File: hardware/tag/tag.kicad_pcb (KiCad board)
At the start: 2 copper layers, 50 x 52 mm, 109 parts, among them J1 USB_C_Receptacle_USB2.0_16P, J2 BATTERY, J3 UART, J4 I2C, J5 STM SWD, J6 ADC, J7 BLE SWD, J8 SOURCE, SW1 RESET, SW2 BOOT, SW3 USER, U1 ICM-45686, U2 TPS63070RNMR, U3 BQ24075RGT, U4 USBLC6-2SC6, U5 FSC-BT630, U6 STM32F411CEUx, U7 DWM1000, Y1 NX3215SA-32.768kHz(DNP), Y2 NX3225SA-24MHz

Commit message: refactor(hw): iterate on tag rev 0.2 design
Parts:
- removed C14: 22u, Capacitor_SMD:C_0805_2012Metric_Pad1.18x1.45mm_HandSolder
- removed C5: 1u, Capacitor_SMD:C_0805_2012Metric_Pad1.18x1.45mm_HandSolder
- removed C6, C7: 4.7u, Capacitor_SMD:C_0805_2012Metric_Pad1.18x1.45mm_HandSolder
- removed D1: RED, LED_SMD:LED_0603_1608Metric_Pad1.05x0.95mm_HandSolder
- removed D2: YELLOW, LED_SMD:LED_0603_1608Metric_Pad1.05x0.95mm_HandSolder
- removed R18, R9: 6k, Resistor_SMD:R_0603_1608Metric_Pad0.98x0.95mm_HandSolder
- removed R2: 3.1k, Resistor_SMD:R_0603_1608Metric_Pad0.98x0.95mm_HandSolder
- removed R3: 3.56k, Resistor_SMD:R_0603_1608Metric_Pad0.98x0.95mm_HandSolder
- removed R8: 10k, Resistor_SMD:R_0603_1608Metric_Pad0.98x0.95mm_HandSolder
- removed U3: BQ24075RGT, Package_DFN_QFN:VQFN-16-1EP_3x3mm_P0.5mm_EP1.6x1.6mm
- added C10: 1u, Capacitor_SMD:C_0805_2012Metric_Pad1.18x1.45mm_HandSolder, F.Cu at (51.0, 91.2)
- added C12: DNP, Capacitor_SMD:C_01005_0402Metric, F.Cu at (79.7, 74.7)
- added C34: 47n, Capacitor_SMD:C_0603_1608Metric, F.Cu at (47.7, 94.0)
- added C35: 4.7u, Capacitor_SMD:C_0805_2012Metric, F.Cu at (45.0, 95.0)
- added C36: 20u, Capacitor_SMD:C_0805_2012Metric, F.Cu at (56.4, 96.2)
- added C37: 10u, Capacitor_SMD:C_0805_2012Metric, F.Cu at (45.0, 99.1)
- added C8: DNP, Capacitor_SMD:C_01005_0402Metric, F.Cu at (79.7, 77.2)
- added D9: YELLOW, LED_SMD:LED_0603_1608Metric_Pad1.05x0.95mm_HandSolder, F.Cu at (51.7, 87.0)
- added J6: BLE_Conn, Connector_Coaxial:U.FL_Hirose_U.FL-R-SMT-1_Vertical, F.Cu at (76.8, 78.0)
- added L2: DNP, Inductor_SMD:L_0402_1005Metric, F.Cu at (79.9, 76.0)
- added L3: 1u, Inductor_SMD:L_Sunlord_SWPA4020S, F.Cu at (60.0, 91.2)
- added R25: 2.2k, Resistor_SMD:R_0603_1608Metric_Pad0.98x0.95mm_HandSolder, F.Cu at (48.0, 87.0)
- added R26: 10K, Resistor_SMD:R_0603_1608Metric_Pad0.98x0.95mm_HandSolder, F.Cu at (52.2, 98.2)
- added R27: DNP, Resistor_SMD:R_0603_1608Metric_Pad0.98x0.95mm_HandSolder, F.Cu at (47.7, 96.0)
- added U8: BQ25628RYKR, Other_Footprint:IC_BQ25628RYKR, F.Cu at (51.6, 95.4)
- C15: value DNP -> 22u
- D3: value YELLOW -> GREEN
- D4: value GREEN -> RED
- SW2: value BOOT -> PWR; footprint Button_Switch_SMD:SW_SPDT_PCM12 -> Button_Switch_SMD:SW_Push_1P1T-MP_NO_Horizontal_Alps_SKRTLAE010
- U5: footprint Other_Footprint:FSC-BT630 -> other_footprint:FSC-BT630
- moved SW2 22.1 mm to (57.4, 100.5), turned to 0 degrees
- moved R14 18.2 mm to (56.0, 85.5)
- moved TP3 7.84 mm to (78.0, 90.0)
- moved TP6 6.78 mm to (63.6, 91.1)
- moved D8 5.38 mm to (72.2, 76.1), turned to 90 degrees
- moved C1 4.32 mm to (62.4, 96.0), turned to -90 degrees
- moved R5 4.04 mm to (64.6, 99.4)
- moved C26 3.95 mm to (71.9, 60.5), turned to 0 degrees
- moved C4 3.68 mm to (64.3, 94.2)
- moved C15 3.64 mm to (73.8, 90.2)
- moved C11 3.63 mm to (73.7, 95.1)
- moved C13 3.63 mm to (73.7, 92.7)
- moved R10 3.63 mm to (73.7, 97.4)
- moved R11 3.63 mm to (73.7, 99.8)
- moved C27 3.56 mm to (72.1, 58.7), turned to 0 degrees
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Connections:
- net /SYS renamed SYS
- R14 pad 1: Net-(SW2-B) -> GND
- R19 pad 2: Net-(U5-P0.02/AIN0) -> Net-(U5-P0.03)
- SW2 pad 2: Net-(SW2-B) -> Net-(R26-Pad1)
- U5 pad 1: +3.3V -> /BLE_RX
- U5 pad 10: GND -> /BLE_SWDIO
- U5 pad 11: Net-(U5-P0.02/AIN0) -> unconnected-(U5-P0.30-Pad11)
- U5 pad 15: unconnected-(U5-P0.06-Pad15) -> Net-(U5-P0.03)
- U5 pad 19: unconnected-(U5-P0.10/NFC2-Pad19) -> GND
- U5 pad 20: unconnected-(U5-P0.11-Pad20) -> Net-(U5-EXT_ANT)
- U5 pad 3: /BLE_RX -> unconnected-(U5-I2C_SDA-Pad3)
- U5 pad 7: /BLE_SWDCLK -> +3.3V
- U5 pad 8: /BLE_SWDIO -> GND
- U5 pad 9: GND -> /BLE_SWDCLK
- U6 pad 29: /PA8 / TIM1_CH1 -> /PM_SCL
- U6 pad 38: /PA15 / TIM2_CH1 -> /LED_PM
- U6 pad 40: /PB4/TIM3_CH1 -> /PM_SDA
- U6 pad 42: /PB6 / TIM4_CH1 -> unconnected-(U6-PB6-Pad42)
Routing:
- net /PM_SCL: track 0.00 -> 25.3 mm, vias 0 -> 2
- net SYS: track 30.8 -> 9.78 mm, vias 0 -> 6
- net Net-(U6-BOOT0): track 24.2 -> 3.25 mm, vias 2 -> 0
- net /PM_SDA: track 0.00 -> 15.2 mm, vias 0 -> 2
- net /PGOOD: track 14.8 -> 0.00 mm, vias 2 -> 0
- net /CHG: track 10.9 -> 0.00 mm, vias 2 -> 0
- net /LED_PM: track 0.00 -> 10.1 mm
- net GND: track 25.0 -> 16.1 mm, vias 321 -> 299
- net +3.3V: track 221.2 -> 214.4 mm
- net +BATT: track 9.33 -> 3.43 mm, vias 0 -> 12
- net Net-(U8-REGN): track 0.00 -> 5.55 mm
- net Net-(R26-Pad1): track 0.00 -> 5.43 mm
- net Net-(U5-P0.02/AIN0): track 4.68 -> 0.00 mm
- net Net-(U8-SW): track 0.00 -> 4.20 mm, vias 0 -> 2
- net Net-(U8-BTST): track 0.00 -> 3.59 mm
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- added copper zone on B.Cu, net +BATT
- added copper zone on F.Cu, net +BATT
- added copper zone on F.Cu, net Net-(U8-SW)
- added copper zone on B.Cu, net SYS
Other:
- board text added: "${REFERENCE}"
- board text added: "3V3 RX TX GND"
- board text added: "BOARD: TAG REV v1.1"
- board text removed: "BOARD: TAG REV v1.0"
- board text removed: "GND TX RX 3V3"

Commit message: update(hw): release tag revision 0.2
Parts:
- removed the C10 at (51.0, 91.2)
- removed the C15 at (73.8, 90.2)
- removed the C3 at (60.4, 96.0)
- removed C34: 47n, Capacitor_SMD:C_0603_1608Metric
- removed C35: 4.7u, Capacitor_SMD:C_0805_2012Metric
- removed C36: 20u, Capacitor_SMD:C_0805_2012Metric
- removed C37: 10u, Capacitor_SMD:C_0805_2012Metric
- removed L3: 1u, Inductor_SMD:L_Sunlord_SWPA4020S
- removed the R26 at (52.2, 98.2)
- removed R27: DNP, Resistor_SMD:R_0603_1608Metric_Pad0.98x0.95mm_HandSolder
- removed the SW2 at (57.4, 100.5)
- removed the TP6 at (63.6, 91.1)
- removed the U8 at (51.6, 95.4)
- added C14: 22u, Capacitor_SMD:C_0805_2012Metric_Pad1.18x1.45mm_HandSolder, F.Cu at (73.8, 90.2)
- added C4: 100n, Capacitor_SMD:C_0603_1608Metric_Pad1.08x0.95mm_HandSolder, F.Cu at (46.1, 96.2)
- added C6: 1u, Capacitor_SMD:C_0805_2012Metric_Pad1.18x1.45mm_HandSolder, F.Cu at (55.0, 90.6)
- added C7: 1u, Capacitor_SMD:C_0603_1608Metric_Pad1.08x0.95mm_HandSolder, F.Cu at (62.7, 94.0)
- added C8: 4.7u, Capacitor_SMD:C_0805_2012Metric_Pad1.18x1.45mm_HandSolder, F.Cu at (50.0, 98.6)
- added C9: 10u, Capacitor_SMD:C_0805_2012Metric_Pad1.18x1.45mm_HandSolder, F.Cu at (57.7, 92.6)
- added Q1: AO664, Package_SO:TSOP-6_1.65x3.05mm_P0.95mm, F.Cu at (57.7, 95.5)
- added R12: 100k, Resistor_SMD:R_0603_1608Metric_Pad0.98x0.95mm_HandSolder, F.Cu at (61.0, 94.0)
- added R13: 10k, Resistor_SMD:R_0603_1608Metric_Pad0.98x0.95mm_HandSolder, F.Cu at (62.0, 91.5)
- added R14: 10k, Resistor_SMD:R_0603_1608Metric_Pad0.98x0.95mm_HandSolder, F.Cu at (60.2, 97.8)
- added R5: 3.1k, Resistor_SMD:R_0603_1608Metric_Pad0.98x0.95mm_HandSolder, F.Cu at (62.0, 90.0)
- added R6: 3.56k, Resistor_SMD:R_0603_1608Metric_Pad0.98x0.95mm_HandSolder, F.Cu at (51.4, 92.4)
- added R8: 10k, Resistor_SMD:R_0603_1608Metric_Pad0.98x0.95mm_HandSolder, F.Cu at (49.0, 93.3)
- added SW1: PWR, Button_Switch_SMD:SW_Push_1P1T-MP_NO_Horizontal_Alps_SKRTLAE010, F.Cu at (56.0, 100.3)
- added TP3: VSYS, TestPoint:TestPoint_Pad_D1.5mm, F.Cu at (58.5, 89.8)
- added U1: MAX17048G_T10, Package_SON:SON-8-1EP_3x2mm_P0.5mm_EP1.4x1.6mm, F.Cu at (46.6, 93.5)
- added U5: BQ24075RGT, Package_DFN_QFN:VQFN-16-1EP_3x3mm_P0.5mm_EP1.6x1.6mm, F.Cu at (53.3, 95.5)
- D3: value GREEN -> YELLOW
- D4: renamed from D9; value YELLOW -> GREEN
- D5: renamed from D4; value RED -> GREEN
- J9: renamed from J6; value ADC -> I2C
- TP2: renamed from TP3; footprint TestPoint:TestPoint_Pad_D2.0mm -> TestPoint:TestPoint_Pad_1.5x1.5mm
- TP5: renamed from TP4; footprint TestPoint:TestPoint_Pad_D2.0mm -> TestPoint:TestPoint_Pad_1.5x1.5mm
- moved C2 5.82 mm to (63.9, 98.0)
- moved C15 3.04 mm to (43.0, 74.4), turned to 180 degrees
- moved TP16 2.19 mm to (39.5, 69.8)
- moved TP7 2.16 mm to (45.4, 98.3)
- moved J4 2.00 mm to (35.0, 92.5), turned to 90 degrees
- moved C1 2.00 mm to (62.0, 98.0)
- moved R1 1.58 mm to (67.7, 99.5)
- moved R11 1.53 mm to (69.3, 99.5)
- moved C10 1.51 mm to (45.6, 75.1), turned to -90 degrees
- moved C5 1.49 mm to (70.9, 99.5)
- moved R2 1.49 mm to (66.1, 99.5)
- moved J6 1.45 mm to (78.7, 84.8)
- moved J1 1.38 mm to (34.0, 79.5)
- moved R3 1.38 mm to (40.3, 84.5)
- moved R4 1.38 mm to (40.3, 75.1)
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- renumbered C31 to C10, C13 to C12, C32 to C13, C33 to C15, C27 to C16, C26 to C17, C16 to C18, C17 to C19, C18 to C20, C19 to C21, C20 to C22, C21 to C23, C22 to C24, C12 to C25, C8 to C26, C23 to C27, C24 to C28, C25 to C29, C4 to C3, C28 to C30, C29 to C31, C30 to C32, C9 to C5, D7 to D1, D8 to D2, D5 to D6, D6 to D7, H3 to H1, H4 to H2, H2 to H3, H1 to H4, J6 to J3, J8 to J4, J4 to J6, J3 to J7, J7 to J8, R4 to R1, R11 to R10, R12 to R11, R13 to R15, R19 to R16, R16 to R18, R25 to R19, R5 to R2, R15 to R20, R1 to R21, R20 to R22, R21 to R23, R22 to R25, R14 to R26, R7 to R3, R6 to R4, R23 to R7, R10 to R9, SW1 to SW2, TP8 to TP10, TP9 to TP11, TP14 to TP12, TP10 to TP13, TP11 to TP14, TP5 to TP15, TP12 to TP4, TP2 to TP6, TP15 to TP7, TP13 to TP8, TP7 to TP9, U4 to U2, U1 to U3, U2 to U4, U5 to U6, U6 to U7, U7 to U8
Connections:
- net SYS renamed /LOAD
- J4 pad 1: VBUS -> GND
- J4 pad 2: GND -> VBUS
- J5 pad 1: +3.3V -> /STM_SWDCLK
- J5 pad 2: /STM_SWDCLK -> /STM_SWDIO
- J5 pad 3: /STM_SWDIO -> GND
- J5 pad 4: GND -> +3.3V
- J6 pad 2: /PB8 / I2C1_SCL -> GND
- J6 pad 3: /PB9 / I2C1_SDA -> /PB8 / I2C1_SCL
- J6 pad 4: GND -> /PB9 / I2C1_SDA
- J7 pad 2: /PA10 / UART1_RX -> GND
- J7 pad 3: /PA9 / UART1_TX -> /PA10 / UART1_RX
- J7 pad 4: GND -> /PA9 / UART1_TX
- J8 pad 1: +3.3V -> /BLE_SWDCLK
- J8 pad 3: /BLE_SWDCLK -> /BLE_RST
- J8 pad 4: /BLE_RST -> GND
- J8 pad 5: GND -> +3.3V
- J9 pad 2: /PB1 / ADC_IN9 -> GND
- J9 pad 3: /PB0 / ADC_IN8 -> /PB1 / ADC_IN9
- J9 pad 4: GND -> /PB0 / ADC_IN8
- R26 pad 1: GND -> Net-(U7-BOOT0)
- R26 pad 2: Net-(U6-BOOT0) -> GND
- U7 pad 44: Net-(U6-BOOT0) -> Net-(U7-BOOT0)
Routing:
- net /PM_SCL: track 25.3 -> 2.87 mm, vias 2 -> 1
- net /PB9 / I2C1_SDA: track 23.3 -> 41.7 mm, vias 3 -> 4
- net /PB8 / I2C1_SCL: track 23.2 -> 41.4 mm, vias 3 -> 4
- net /SYS: track 0.00 -> 16.3 mm
- net /PM_SDA: track 15.2 -> 0.00 mm, vias 2 -> 0
- net Net-(C7-Pad2): track 0.00 -> 14.0 mm, vias 0 -> 2
- net Net-(Q1A-G1): track 0.00 -> 11.2 mm, vias 0 -> 2
- net GND: track 16.1 -> 25.1 mm, vias 299 -> 352
- net Net-(U5-ILIM): track 0.00 -> 8.85 mm, vias 0 -> 2
- net Net-(Q1B-G2): track 0.00 -> 8.41 mm
- net Net-(U8-REGN): track 5.55 -> 0.00 mm
- net Net-(R26-Pad1): track 5.43 -> 0.00 mm
- net +3.3V: track 214.4 -> 209.2 mm
- net Net-(U8-SW): track 4.20 -> 0.00 mm, vias 2 -> 0
- net /LOAD: track 9.78 -> 5.94 mm, vias 6 -> 0
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- added copper zone on F.Cu, net /SYS
- removed copper zone on B.Cu, net +BATT
- removed copper zone on B.Cu, net /LOAD
- removed copper zone on F.Cu, net Net-(U8-SW)
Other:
- board text added: "3V3 GND AUX1 AUX2"
- board text added: "GND 3V3 RX TX"
- board text added: "SDA SCL GND 3V3"
- board text added: "SWDCLK SWDIO GND 3V3"
- board text added: "SWDIO SWCK RST GND 3V3"
- board text removed: "${REFERENCE}"
- board text removed: "3V3 RX TX GND"
- board text removed: "GND ADC1 ADC2 3V3"
- board text removed: "GND SDA SCL 3V3"
- board text removed: "GND SWDIO SWCK 3V3"

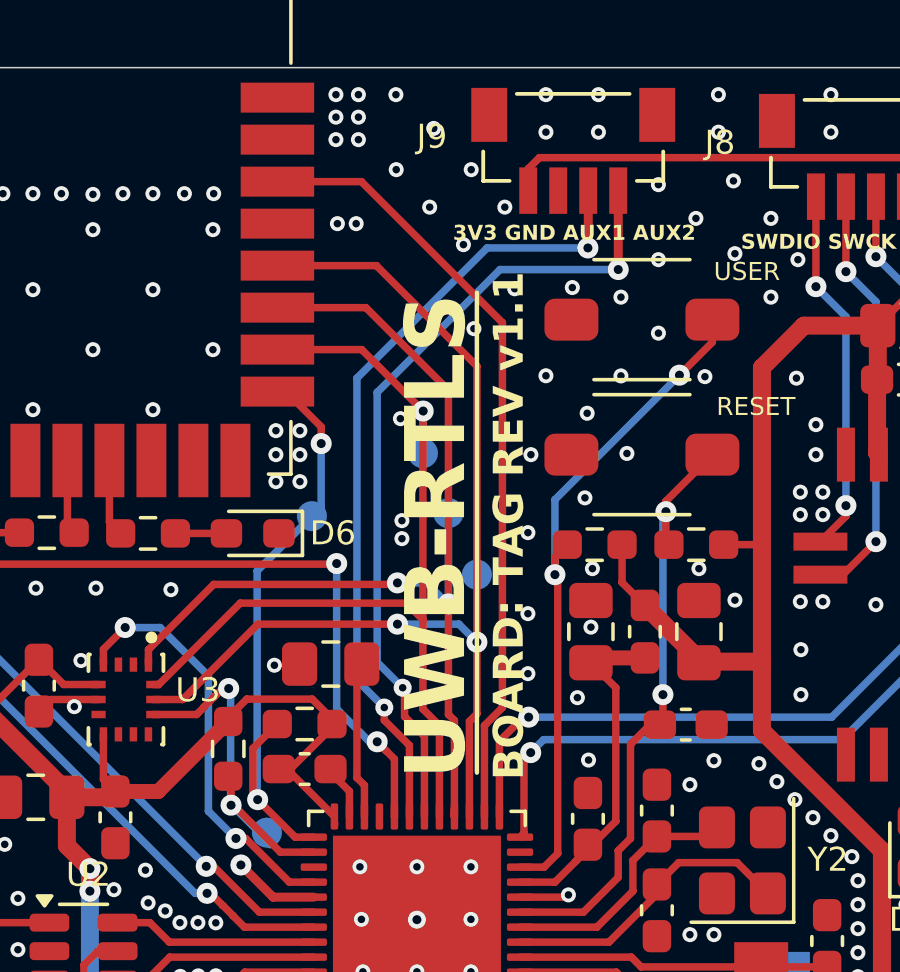
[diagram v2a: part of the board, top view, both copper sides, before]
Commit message: feat: Implement UWB IRQ on PA4 with event-driven RX
- Configure PA4 as EXTI4 rising edge interrupt
- Add EXTI4_IRQHandler to forward interrupts to BSP
- Implement IRQ event flag system in bsp_uwb (on_irq, wait, clear APIs)
- Route PA4 EXTI callback in bsp_io to bsp_uwb_on_irq()
- Update hardware PCB production labels (TAG v1.1, REL 2025-02-22)
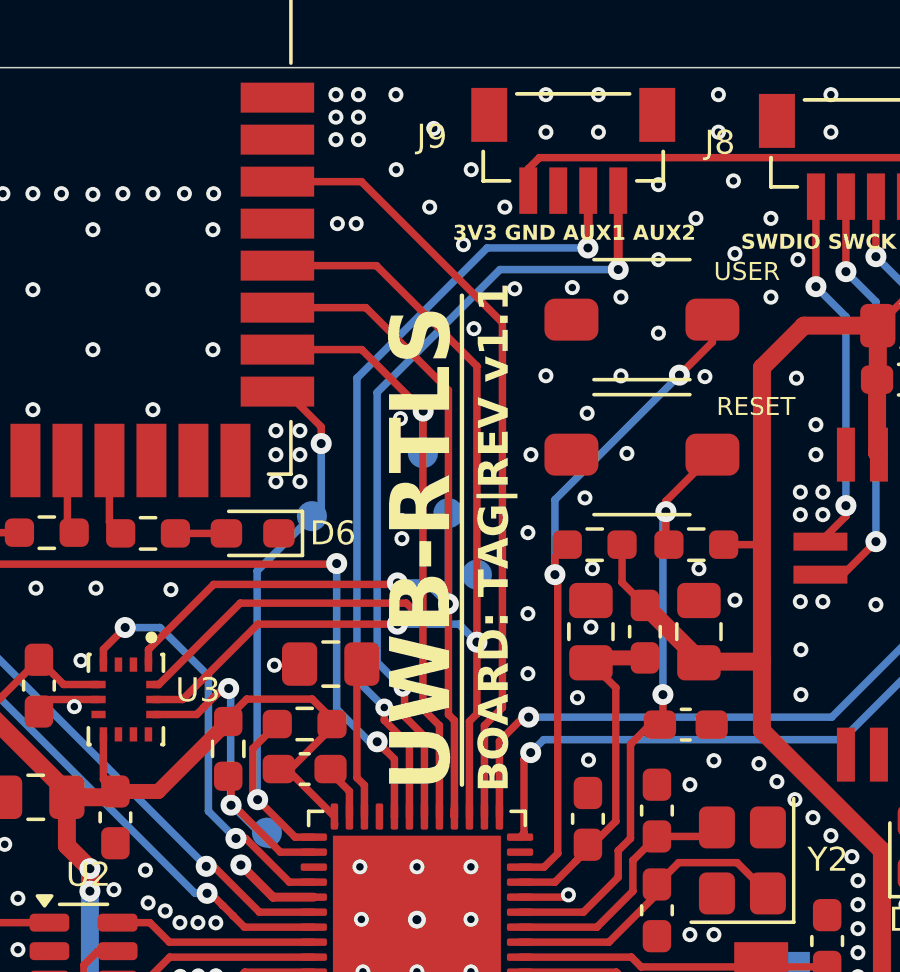
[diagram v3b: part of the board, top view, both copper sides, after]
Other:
- board text added: "BOARD: TAG|REV v1.1"
- board text added: "ID:"
- board text added: "PRODUCTION BOARD REL: 2025-02-22"
- board text removed: "BOARD: TAG REV v1.1"
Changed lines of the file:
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@@
 	)
 	(gr_line
-		(start 57.7 73.6)
-		(end 57.7 57.6)
+		(start 57.2 74)
+		(end 57.2 57.7)
 		(stroke
 			(width 0.15)
@@
 		(layer "F.SilkS")
 	)
+	(gr_rect
+		(start 64.3 99.25)
+		(end 73.3 100.5)
+		(stroke
+			(width 0.1)
+			(type solid)
+		)
+		(fill yes)
+		(layer "B.SilkS")
+	)
 	(gr_arc
 		(start 78.8 50.1)
@@
 	)
 	(gr_text "UWB-RTLS\n"
-		(at 57.515 73.82 90)
+		(at 57.015 74.22 90)
 		(layer "F.SilkS")
 		(effects
@@
 		)
 	)
-	(gr_text "BOARD: TAG REV v1.1"
-		(at 59.35 73.845 90)
+	(gr_text "BOARD: TAG|REV v1.1"
+		(at 58.85 74.245 90)
 		(layer "F.SilkS")
 		(effects
@@
 		)
 	)
+	(gr_text "PRODUCTION BOARD\nREL: 2025-02-22\n"
+		(at 75.4 97.7 0)
+		(layer "B.SilkS")
+		(effects
+			(font
+				(size 0.8 0.8)
+				(thickness 0.17)
+				(bold yes)
+			)
+			(justify left mirror)
+		)
+	)
+	(gr_text "ID:"
+		(at 75.4 99.9 0)
+		(layer "B.SilkS")
+		(effects
+			(font
+				(size 0.8 0.8)
+				(thickness 0.17)
+				(bold yes)
+			)
+			(justify left mirror)
+		)
+	)

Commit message: wip
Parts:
- added F1: Polyfuse_Small, Fuse:Fuse_1206_3216Metric, F.Cu at (49.9, 90.5)
- added J10: Conn_01x02, Connector_Wire:SolderWire-0.1sqmm_1x02_P3.6mm_D0.4mm_OD1mm, F.Cu at (38.8, 99.5)
- C25, C26: footprint Capacitor_SMD:C_01005_0402Metric -> Capacitor_SMD:C_0402_1005Metric
- moved D5 28.3 mm to (79.1, 96.3)
- moved D4 28.3 mm to (79.1, 94.1)
- moved D3 28.2 mm to (79.1, 92.0)
- moved TP8 27.5 mm to (43.1, 69.0)
- moved D2 15.3 mm to (79.1, 89.8), turned to 180 degrees
- moved TP2 9.90 mm to (68.8, 86.2)
- moved R19 5.53 mm to (53.0, 84.1)
- moved R20 5.22 mm to (53.0, 87.2)
- moved R18 5.15 mm to (53.0, 85.7)
- moved TP4 2.10 mm to (72.2, 68.5)
- moved TP7 2.07 mm to (47.4, 98.1)
- moved J2 1.79 mm to (42.9, 99.9)
- moved C4 1.19 mm to (47.2, 96.0), turned to 0 degrees
- moved TP11 1.15 mm to (74.2, 68.8)
- moved F2 0.62 mm to (34.4, 64.0)
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- renumbered F1 to F2
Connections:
- C6 pad 2: VBUS -> /VBUS_PROTECT
- D3 pad 1: /LED_USR -> GND
- D4 pad 1: GND -> /CHG
- R18 pad 2: +3.3V -> /LED_USR
- R19 pad 2: /LED_PM -> +3.3V
- U5 pad 13: VBUS -> /VBUS_PROTECT
- U5 pad 9: unconnected-(U5-~{CHG}-Pad9) -> /CHG
- U7 pad 38: /LED_PM -> unconnected-(U7-PA15-Pad38)
- U7 pad 39: unconnected-(U7-PB3-Pad39) -> /CHANGER SENSE
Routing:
- net /CHG: track 0.00 -> 29.6 mm, vias 0 -> 2
- net Net-(D4-A): track 1.94 -> 29.7 mm, vias 0 -> 2
- net Net-(D5-A): track 2.07 -> 29.5 mm, vias 0 -> 2
- net Net-(D3-A): track 2.08 -> 27.6 mm, vias 0 -> 2
- net Net-(D2-A): track 2.41 -> 15.8 mm, vias 0 -> 2
- net /LED_PM: track 9.46 -> 0.00 mm
- net /BLE_TX: track 28.1 -> 25.9 mm
- net /BLE_RX: track 29.2 -> 27.4 mm
- net GND: track 25.1 -> 24.0 mm, vias 352 -> 370
- net Net-(Q1A-G1): track 11.2 -> 10.3 mm
- net /PB9 / I2C1_SDA: track 41.7 -> 42.5 mm
- net /SYS: track 16.3 -> 15.6 mm
- net /PB8 / I2C1_SCL: track 41.4 -> 40.9 mm
- net Net-(J1-D--PadA7): track 7.40 -> 7.90 mm
- net Net-(J1-D+-PadA6): track 8.73 -> 9.23 mm
- added copper zone on F.Cu, net /VBUS_PROTECT
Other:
- board text added: "BOARD: TAG|REV: v1.2"
- board text added: "PRODUCTION BOARD REL: 2025-02-25"
- board text removed: "BOARD: TAG|REV v1.1"
- board text removed: "PRODUCTION BOARD REL: 2025-02-22"
